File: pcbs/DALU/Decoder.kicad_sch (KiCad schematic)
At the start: 16 parts, among them U301 74HC138

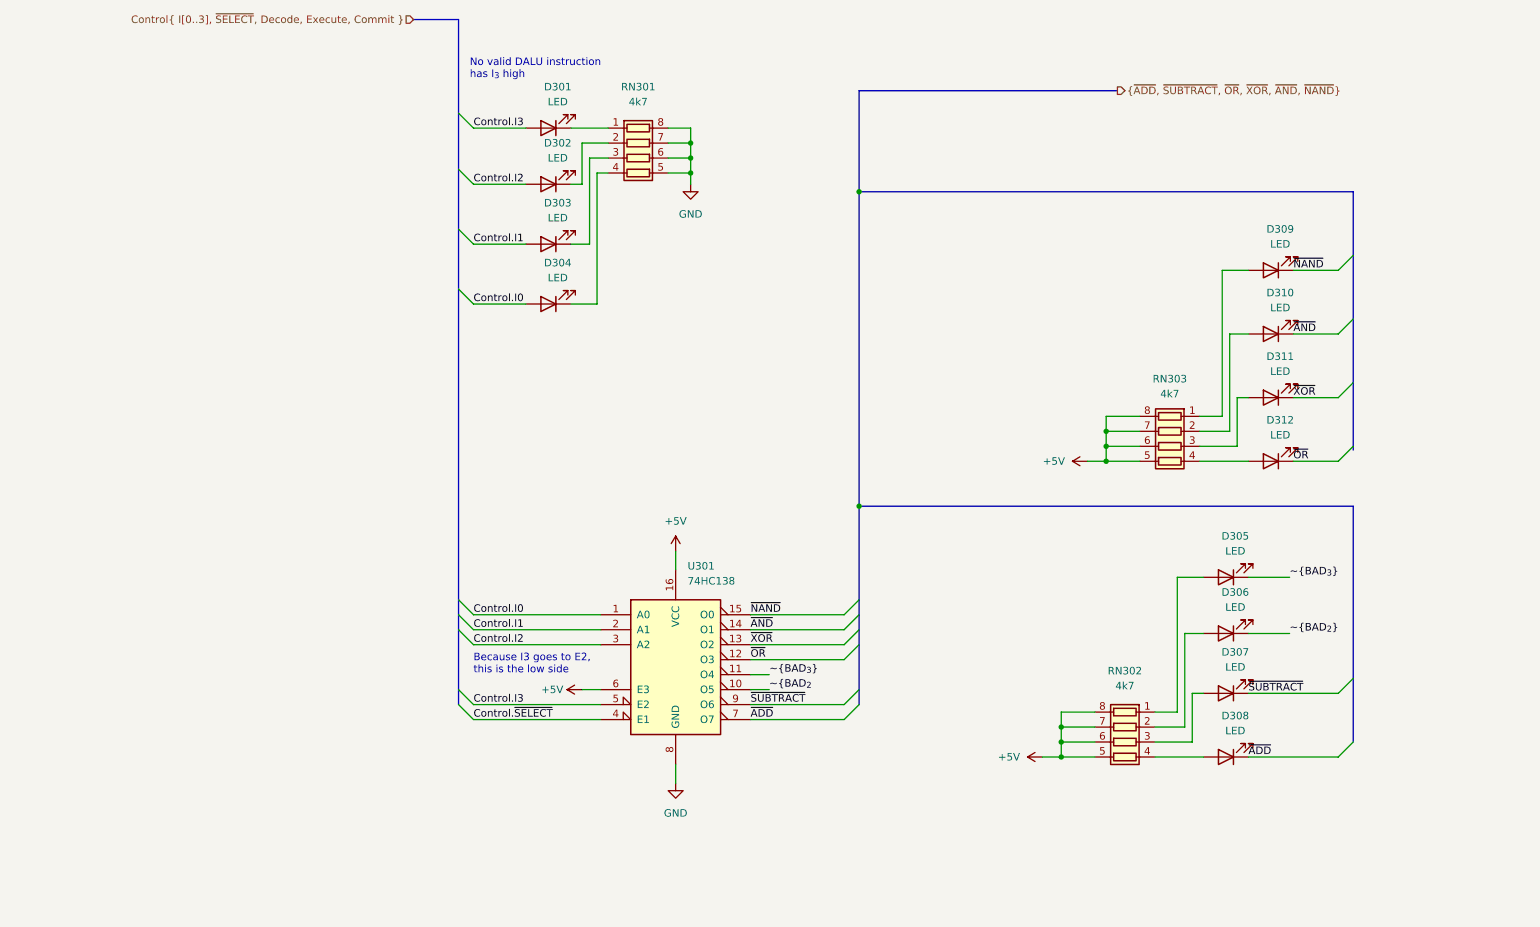
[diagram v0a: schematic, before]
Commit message: Starting to connect up control wires
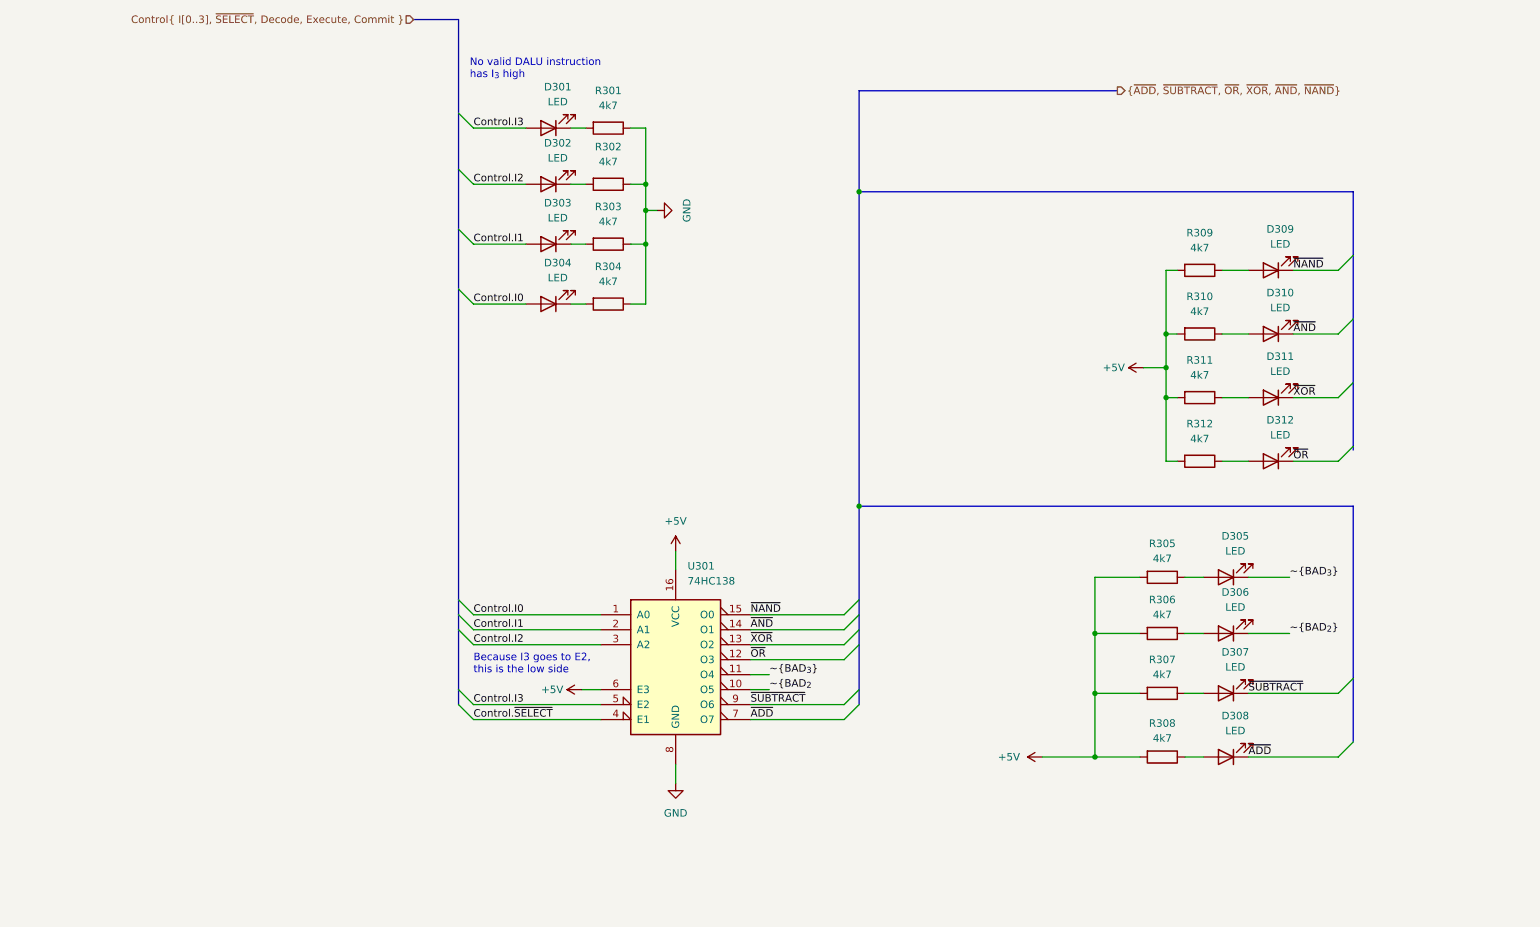
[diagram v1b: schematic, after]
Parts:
- removed RN301, RN302, RN303: 4k7, Resistor_SMD:R_Array_Convex_4x0603, symbol Device:R_Pack04
- added R301, R302, R303, R304, R305, R306, R307, R308, R309, R310, R311, R312: 4k7, Resistor_SMD:R_0603_1608Metric, symbol Device:R
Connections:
- net +5V: now also R305.2, R306.2, R307.2, R308.2, R309.2, R310.2, R311.2, R312.2
- net GND: now also R301.1, R302.1, R303.1, R304.1
- net at D306.2 (A): now also R306.1
- net at D305.2 (A): now also R305.1
- net at D303.1 (K): now also R303.2
- net at D308.2 (A): now also R308.1
- net at D312.2 (A): now also R312.1
- net at D301.1 (K): now also R301.2
- net at D309.2 (A): now also R309.1
- net at D310.2 (A): now also R310.1
- net at D311.2 (A): now also R311.1
- net at D302.1 (K): now also R302.2
- net at D304.1 (K): now also R304.2
- net at D307.2 (A): now also R307.1

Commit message: Finish preliminary routing
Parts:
- added C301: 100n, Capacitor_SMD:C_0603_1608Metric, symbol Device:C
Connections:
- net +5V: now also C301.1
- net GND: now also C301.2
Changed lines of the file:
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@@
+    (stroke (width 0) (type default) (color 0 0 0 0))
+  )
+  (wire (pts (xy 40.64 165.735) (xy 40.64 167.005))
     (stroke (width 0) (type default) (color 0 0 0 0))
   )
@@
     (stroke (width 0) (type default) (color 0 0 0 0))
   )
+  (wire (pts (xy 40.64 154.94) (xy 45.72 154.94))
+    (stroke (width 0) (type default) (color 0 0 0 0))
+  )
   (wire (pts (xy 193.675 74.93) (xy 193.675 80.645))
     (stroke (width 0) (type default) (color 0 0 0 0))
@@
     (stroke (width 0) (type default) (color 0 0 0 0))
   )
+  (wire (pts (xy 40.64 167.005) (xy 46.355 167.005))
+    (stroke (width 0) (type default) (color 0 0 0 0))
+  )
   (bus (pts (xy 73.66 122.555) (xy 73.66 125.095))
     (stroke (width 0) (type default) (color 0 0 0 0))
@@
   )
   (wire (pts (xy 76.2 127.635) (xy 97.79 127.635))
+    (stroke (width 0) (type default) (color 0 0 0 0))
+  )
+  (wire (pts (xy 40.64 158.115) (xy 40.64 154.94))
     (stroke (width 0) (type default) (color 0 0 0 0))
   )
@@
   (symbol (lib_id "power:GND") (at 110.49 151.13 0) (unit 1)
     (in_bom yes) (on_board yes) (fields_autoplaced)
-    (property "Reference" "#PWR0304" (id 0) (at 110.49 157.48 0)
+    (property "Reference" "#PWR0306" (id 0) (at 110.49 157.48 0)
       (effects (font (size 1.27 1.27)) hide)
     )
@@
     )
     (pin "1")
+  )
+  (symbol (lib_id "Device:C") (at 40.64 161.925 0) (unit 1)
+    (in_bom yes) (on_board yes) (fields_autoplaced)
+    (property "Reference" "C301" (id 0) (at 44.45 160.6549 0)
+      (effects (font (size 1.27 1.27)) (justify left))
+    )
+    (property "Value" "100n" (id 1) (at 44.45 163.1949 0)
+      (effects (font (size 1.27 1.27)) (justify left))
+    )
+    (property "Footprint" "Capacitor_SMD:C_0603_1608Metric" (id 2) (at 41.6052 165.735 0)
+      (effects (font (size 1.27 1.27)) hide)
+    )
+    (property "Datasheet" "https://datasheet.lcsc.com/lcsc/1809301912_YAGEO-CC0603KRX7R9BB104_C14663.pdf" (id 3) (at 40.64 161.925 0)
+      (effects (font (size 1.27 1.27)) hide)
+    )
+    (property "LCSC" "C14663" (id 4) (at 40.64 161.925 0)
+      (effects (font (size 1.27 1.27)) hide)
+    )
+    (pin "1")
+    (pin "2")
   )
   (symbol (lib_id "Device:R") (at 193.04 116.205 270) (unit 1)
@@
     (pin "2")
   )
+  (symbol (lib_id "power:GND") (at 46.355 167.005 0) (unit 1)
+    (in_bom yes) (on_board yes) (fields_autoplaced)
+    (property "Reference" "#PWR0302" (id 0) (at 46.355 173.355 0)
+      (effects (font (size 1.27 1.27)) hide)
+    )
+    (property "Value" "GND" (id 1) (at 46.355 172.085 0))
+    (property "Footprint" "" (id 2) (at 46.355 167.005 0)
+      (effects (font (size 1.27 1.27)) hide)
+    )
+    (property "Datasheet" "" (id 3) (at 46.355 167.005 0)
+      (effects (font (size 1.27 1.27)) hide)
+    )
+    (pin "1")
+  )
   (symbol (lib_id "power:+5V") (at 189.865 80.645 90) (unit 1)
     (in_bom yes) (on_board yes) (fields_autoplaced)
-    (property "Reference" "#PWR0306" (id 0) (at 193.675 80.645 0)
+    (property "Reference" "#PWR0308" (id 0) (at 193.675 80.645 0)
       (effects (font (size 1.27 1.27)) hide)
     )
@@
   (symbol (lib_id "power:+5V") (at 172.72 146.685 90) (unit 1)
     (in_bom yes) (on_board yes) (fields_autoplaced)
-    (property "Reference" "#PWR0305" (id 0) (at 176.53 146.685 0)
+    (property "Reference" "#PWR0307" (id 0) (at 176.53 146.685 0)
       (effects (font (size 1.27 1.27)) hide)
     )
@@
   (symbol (lib_id "power:+5V") (at 110.49 111.76 0) (unit 1)
     (in_bom yes) (on_board yes) (fields_autoplaced)
-    (property "Reference" "#PWR0303" (id 0) (at 110.49 115.57 0)
+    (property "Reference" "#PWR0305" (id 0) (at 110.49 115.57 0)
       (effects (font (size 1.27 1.27)) hide)
     )
@@
   (symbol (lib_id "power:+5V") (at 94.615 135.255 90) (unit 1)
     (in_bom yes) (on_board yes) (fields_autoplaced)
-    (property "Reference" "#PWR0301" (id 0) (at 98.425 135.255 0)
+    (property "Reference" "#PWR0303" (id 0) (at 98.425 135.255 0)
       (effects (font (size 1.27 1.27)) hide)
     )
@@
   (symbol (lib_id "power:GND") (at 107.315 53.975 90) (unit 1)
     (in_bom yes) (on_board yes) (fields_autoplaced)
-    (property "Reference" "#PWR0302" (id 0) (at 113.665 53.975 0)
+    (property "Reference" "#PWR0304" (id 0) (at 113.665 53.975 0)
       (effects (font (size 1.27 1.27)) hide)
     )
@@
     (pin "2")
   )
+  (symbol (lib_id "power:+5V") (at 45.72 154.94 0) (unit 1)
+    (in_bom yes) (on_board yes) (fields_autoplaced)
+    (property "Reference" "#PWR0301" (id 0) (at 45.72 158.75 0)
+      (effects (font (size 1.27 1.27)) hide)
+    )
+    (property "Value" "+5V" (id 1) (at 45.72 149.86 0))
+    (property "Footprint" "" (id 2) (at 45.72 154.94 0)
+      (effects (font (size 1.27 1.27)) hide)
+    )
+    (property "Datasheet" "" (id 3) (at 45.72 154.94 0)
+      (effects (font (size 1.27 1.27)) hide)
+    )
+    (pin "1")
+  )
 )

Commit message: Sending for production
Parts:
- D301, D305, D306: value LED -> RED
- D302, D303, D304, D307, D308, D309, D310, D311, D312: value LED -> GREEN
- U301: now left out of the parts list
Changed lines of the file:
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@@
   )
   (symbol (lib_id "74xx:74LS138") (at 110.49 130.175 0) (unit 1)
-    (in_bom yes) (on_board yes) (fields_autoplaced)
+    (in_bom no) (on_board yes) (fields_autoplaced)
     (property "Reference" "U301" (id 0) (at 112.5094 114.3 0)
       (effects (font (size 1.27 1.27)) (justify left))
@@
     (in_bom yes) (on_board yes) (fields_autoplaced)
     (property "Reference" "D306" (id 0) (at 205.4225 118.745 0))
-    (property "Value" "LED" (id 1) (at 205.4225 121.285 0))
+    (property "Value" "RED" (id 1) (at 205.4225 121.285 0))
     (property "Footprint" "LED_SMD:LED_0603_1608Metric" (id 2) (at 203.835 125.73 0)
       (effects (font (size 1.27 1.27)) hide)
@@
     (in_bom yes) (on_board yes) (fields_autoplaced)
     (property "Reference" "D305" (id 0) (at 205.4225 109.22 0))
-    (property "Value" "LED" (id 1) (at 205.4225 111.76 0))
+    (property "Value" "RED" (id 1) (at 205.4225 111.76 0))
     (property "Footprint" "LED_SMD:LED_0603_1608Metric" (id 2) (at 203.835 116.205 0)
       (effects (font (size 1.27 1.27)) hide)
@@
     (in_bom yes) (on_board yes) (fields_autoplaced)
     (property "Reference" "D303" (id 0) (at 90.4875 52.705 0))
-    (property "Value" "LED" (id 1) (at 90.4875 55.245 0))
+    (property "Value" "GREEN" (id 1) (at 90.4875 55.245 0))
     (property "Footprint" "LED_SMD:LED_0603_1608Metric" (id 2) (at 88.9 59.69 0)
       (effects (font (size 1.27 1.27)) hide)
@@
     (in_bom yes) (on_board yes) (fields_autoplaced)
     (property "Reference" "D308" (id 0) (at 205.4225 139.7 0))
-    (property "Value" "LED" (id 1) (at 205.4225 142.24 0))
+    (property "Value" "GREEN" (id 1) (at 205.4225 142.24 0))
     (property "Footprint" "LED_SMD:LED_0603_1608Metric" (id 2) (at 203.835 146.685 0)
       (effects (font (size 1.27 1.27)) hide)
@@
     (in_bom yes) (on_board yes) (fields_autoplaced)
     (property "Reference" "D312" (id 0) (at 213.0425 89.535 0))
-    (property "Value" "LED" (id 1) (at 213.0425 92.075 0))
+    (property "Value" "GREEN" (id 1) (at 213.0425 92.075 0))
     (property "Footprint" "LED_SMD:LED_0603_1608Metric" (id 2) (at 211.455 96.52 0)
       (effects (font (size 1.27 1.27)) hide)
@@
     (in_bom yes) (on_board yes) (fields_autoplaced)
     (property "Reference" "D301" (id 0) (at 90.4875 33.02 0))
-    (property "Value" "LED" (id 1) (at 90.4875 35.56 0))
+    (property "Value" "RED" (id 1) (at 90.4875 35.56 0))
     (property "Footprint" "LED_SMD:LED_0603_1608Metric" (id 2) (at 88.9 40.005 0)
       (effects (font (size 1.27 1.27)) hide)
@@
     (in_bom yes) (on_board yes) (fields_autoplaced)
     (property "Reference" "D309" (id 0) (at 213.0425 57.15 0))
-    (property "Value" "LED" (id 1) (at 213.0425 59.69 0))
+    (property "Value" "GREEN" (id 1) (at 213.0425 59.69 0))
     (property "Footprint" "LED_SMD:LED_0603_1608Metric" (id 2) (at 211.455 64.135 0)
       (effects (font (size 1.27 1.27)) hide)
@@
     (in_bom yes) (on_board yes) (fields_autoplaced)
     (property "Reference" "D302" (id 0) (at 90.4875 42.545 0))
-    (property "Value" "LED" (id 1) (at 90.4875 45.085 0))
+    (property "Value" "GREEN" (id 1) (at 90.4875 45.085 0))
     (property "Footprint" "LED_SMD:LED_0603_1608Metric" (id 2) (at 88.9 49.53 0)
       (effects (font (size 1.27 1.27)) hide)
@@
     (in_bom yes) (on_board yes) (fields_autoplaced)
     (property "Reference" "D304" (id 0) (at 90.4875 62.865 0))
-    (property "Value" "LED" (id 1) (at 90.4875 65.405 0))
+    (property "Value" "GREEN" (id 1) (at 90.4875 65.405 0))
     (property "Footprint" "LED_SMD:LED_0603_1608Metric" (id 2) (at 88.9 69.85 0)
       (effects (font (size 1.27 1.27)) hide)
@@
   (symbol (lib_id "Device:LED") (at 203.835 135.89 180) (unit 1)
     (in_bom yes) (on_board yes) (fields_autoplaced)
-    (property "Reference" "D307" (id 0) (at 205.4225 128.905 0))
-    (property "Value" "LED" (id 1) (at 205.4225 131.445 0))
+    (property "Reference" "D307" (id 0) (at 205.4225 128.27 0))
+    (property "Value" "GREEN" (id 1) (at 205.4225 130.81 0))
     (property "Footprint" "LED_SMD:LED_0603_1608Metric" (id 2) (at 203.835 135.89 0)
       (effects (font (size 1.27 1.27)) hide)
@@
     (in_bom yes) (on_board yes) (fields_autoplaced)
     (property "Reference" "D311" (id 0) (at 213.0425 78.74 0))
-    (property "Value" "LED" (id 1) (at 213.0425 81.28 0))
+    (property "Value" "GREEN" (id 1) (at 213.0425 81.28 0))
     (property "Footprint" "LED_SMD:LED_0603_1608Metric" (id 2) (at 211.455 85.725 0)
       (effects (font (size 1.27 1.27)) hide)
@@
     (in_bom yes) (on_board yes) (fields_autoplaced)
     (property "Reference" "D310" (id 0) (at 213.0425 67.945 0))
-    (property "Value" "LED" (id 1) (at 213.0425 70.485 0))
+    (property "Value" "GREEN" (id 1) (at 213.0425 70.485 0))
     (property "Footprint" "LED_SMD:LED_0603_1608Metric" (id 2) (at 211.455 74.93 0)
       (effects (font (size 1.27 1.27)) hide)
